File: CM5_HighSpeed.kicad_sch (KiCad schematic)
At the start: 15 parts, among them J12 USB3_A, J13 USB3_A, J15 USB_C_Receptacle_USB2.0, J22 690-019-298-412, J5 Conn_01x22_Female, U12 RT9742SNGV, U6 AP22653W6

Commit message: starting to trace
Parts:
- removed J15: USB_C_Receptacle_USB2.0, Connector_USB:USB_C_Receptacle_GCT_USB4105-xx-A_16P_TopMnt_Horizontal, symbol Connector:USB_C_Receptacle_USB2.0_16P
- added C32, C33: 0.1 µF, Capacitor_SMD:C_0402_1005Metric, symbol Device:C_Small
- added C34, C46: 10u, Capacitor_SMD:C_0402_1005Metric, symbol Device:C
- added C35, C36, C37, C38, C39, C40, C41, C42, C43, C44, C45: 0.1u, Capacitor_SMD:C_0402_1005Metric, symbol Device:C
- added C47, C48: 1u, Capacitor_SMD:C_0402_1005Metric, symbol Device:C
- added C49: 100nF, Capacitor_SMD:C_0402_1005Metric, symbol Device:C
- added C50: 0.1uF, Capacitor_SMD:C_0402_1005Metric, symbol Device:C
- added FB1, FB2: 220 at 100Mhz, libreboard:BEADC1005X55N, symbol Device:FerriteBead_Small
- added J1, J10, J17, J6: 2169890001, libreboard:216989-0001_MOL, symbol MOLEX_2169890001:2169890001
- added J15: USB_C_Receptacle, Connector_USB:USB_C_Receptacle_Molex_105450-0101, symbol Connector:USB_C_Receptacle
- added R25, R26, R34, R35, R36, R37, R38, R39, R40, R41: 5.1 k, Resistor_SMD:R_0402_1005Metric, symbol Device:R_Small
- added R27: 9.53k 1%, Resistor_SMD:R_0402_1005Metric, symbol Device:R_Small
- added R28: 4.7k, Resistor_SMD:R_0402_1005Metric, symbol Device:R_Small
- added R33: 10k, Resistor_SMD:R_0402_1005Metric, symbol Device:R_Small
- added U11: TUSB4041I, Package_QFP:HTQFP-64-1EP_10x10mm_P0.5mm_EP8x8mm_Mask4.4x4.4mm_ThermalVias, symbol Interface_USB:TUSB4041I
- added U13: TLV73311PDBV, Package_TO_SOT_SMD:SOT-23-5, symbol Regulator_Linear:TLV73311PDBV
- added Y1: ECS-2520MV-240-CN-TR, Oscillator:Oscillator_SMD_ECS_2520MV-xxx-xx-4Pin_2.5x2.0mm, symbol Oscillator:ECS-2520MV-xxx-xx
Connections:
- net +3.3v: now also C48.2, C50.2, FB1.1, R25.2, R26.2, R28.1, R33.2, U13.1 (IN), U13.3 (EN), Y1.4 (VDD)
- net GND: now also C32.1, C33.2, C34.2, C35.2, C36.2, C37.2, C38.2, C39.2, C40.2, C41.2, C42.2, C43.2, C44.2, C45.2, C46.2, C47.1, C48.1, C49.1, C50.1, J1.A1 (GND), J1.A12 (GND), J1.B1 (GND), J1.B12 (GND), J10.A1 (GND), J10.A12 (GND), J10.B1 (GND), J10.B12 (GND), J15.A1 (GND), J15.A12 (GND), J15.B1 (GND), J15.B12 (GND), J15.S1 (SHIELD), J17.A1 (GND), J17.A12 (GND), J17.B1 (GND), J17.B12 (GND), J6.A1 (GND), J6.A12 (GND), J6.B1 (GND), J6.B12 (GND), R27.2, R34.2, R35.2, R36.2, R37.2, R38.1, R39.1, R40.1, R41.1, U13.2 (GND), Y1.2 (GND)
- net USB3-0-D_N: now also J15.A7 (D-), J15.B7 (D-); no longer J12.A2 (D-)
- net USB3-0-D_P: now also J15.A6 (D+), J15.B6 (D+); no longer J12.A3 (D+)
- net USB3-0-RX_N: now also J15.B10 (RX1-); no longer J12.A6 (SSRX+)
- net USB3-0-RX_P: now also J15.B11 (RX1+); no longer J12.A5 (SSRX-)
- net USB3-0-TX_N: now also J15.A3 (TX1-); no longer J12.A9 (SSTX+)
- net USB3-0-TX_P: now also J15.A2 (TX1+); no longer J12.A8 (SSTX-)
- net USB3-1-D_N: now also U11.22 (USB_DM_UP); no longer J12.B2 (D-)
- net USB3-1-D_P: now also U11.21 (USB_DP_UP); no longer J12.B3 (D+)
- net USB3-1-RX_N: no longer J12.B6 (SSRX+)
- net USB3-1-RX_P: no longer J12.B5 (SSRX-)
- net USB3-1-TX_N: no longer J12.B9 (SSTX+)
- net USB3-1-TX_P: no longer J12.B8 (SSTX-)
- net VBUS: now also J1.A4 (VBUS), J1.A9 (VBUS), J1.B4 (VBUS), J1.B9 (VBUS), J10.A4 (VBUS), J10.A9 (VBUS), J10.B4 (VBUS), J10.B9 (VBUS), J15.A4 (VBUS), J15.A9 (VBUS), J15.B4 (VBUS), J15.B9 (VBUS), J17.A4 (VBUS), J17.A9 (VBUS), J17.B4 (VBUS), J17.B9 (VBUS), J6.A4 (VBUS), J6.A9 (VBUS), J6.B4 (VBUS), J6.B9 (VBUS), U11.16 (USB_VBUS)
- new net: C39.1, C40.1, C41.1, C42.1, C43.1, C44.1, C45.1, C46.1, FB2.1, U11.19 (VDD), U11.25 (VDD), U11.37 (VDD), U11.45 (VDD), U11.53 (VDD), U11.60 (VDD), U11.63 (VDD)
- new net: R27.1, U11.32 (USB_R1)
- new net: C49.2, R33.1, U11.18 (GRSTz)
- new net: J1.A5 (CC1), R34.1
- new net: J1.A6 (DP1), J1.B6 (DP2), U11.33 (USB_DP_DN1)
- new net: J1.A7 (DN1), J1.B7 (DN2), U11.34 (USB_DM_DN1)
- new net: J1.B5 (CC2), R41.2
- new net: J10.B5 (CC2), R39.2
- new net: J15.A5 (CC1), R25.1
- new net: J17.A5 (CC1), R37.1
- new net: J6.A5 (CC1), R35.1
- new net: J6.B5 (CC2), R40.2
- new net: C34.1, C35.1, C36.1, C37.1, C38.1, FB1.2, U11.2 (VDD33), U11.20 (VDD33), U11.31 (VDD33), U11.48 (VDD33)
- new net: J10.A5 (CC1), R36.1
- new net: J17.B5 (CC2), R38.2
- new net: C33.1, J15.A10 (RX2-)
- new net: C32.2, J15.A11 (RX2+)
- new net: J15.B5 (CC2), R26.1
- new net: C47.2, FB2.2, U13.5 (OUT)
- new net: U11.30 (XI), Y1.3 (OUT)
- new net: R28.2, U11.8 (FULLPWRMGMTz/SMBA1)
- new net: J6.A6 (DP1), J6.B6 (DP2), U11.41 (USB_DP_DN2)
- new net: J6.A7 (DN1), J6.B7 (DN2), U11.42 (USB_DM_DN2)
- new net: J10.A6 (DP1), J10.B6 (DP2), U11.49 (USB_DP_DN3)
- new net: J10.A7 (DN1), J10.B7 (DN2), U11.50 (USB_DM_DN3)
- new net: J17.A6 (DP1), J17.B6 (DP2), U11.56 (USB_DP_DN4)
- new net: J17.A7 (DN1), J17.B7 (DN2), U11.57 (USB_DM_DN4)
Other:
- moved on the sheet: J12, J13

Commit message: fully traced
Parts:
- removed J12, J13: USB3_A, CM5IO:MTCONN_UBAF30-D2011, symbol CM5IO:USB3_A
- added C56, C58, C59: 10u, Capacitor_SMD:C_0805_2012Metric, symbol Device:C
- added C57: 100uF, Capacitor_Tantalum_SMD:CP_EIA-7343-31_Kemet-D, symbol Device:C_Polarized
- added R46: 15K 1%, Resistor_SMD:R_0402_1005Metric, symbol Device:R
- added U15: AP22653W6, Package_TO_SOT_SMD:SOT-23-6, symbol CM5IO:AP2553W6
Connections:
- net +5v: now also C56.1, U15.1 (IN)
- net GND: now also C56.2, C57.2, C58.2, C59.2, R46.2, U15.2 (GND)
- net VBUS_EN: now also U15.3 (EN)
- net VBUS renamed USB2_VBUS
- net USB2_VBUS: no longer J15.A4 (VBUS), J15.A9 (VBUS), J15.B4 (VBUS), J15.B9 (VBUS)
- new net: R46.1, U15.5 (ILIM)
- new net USB3_VBUS: C57.1, C58.1, C59.1, J15.A4 (VBUS), J15.A9 (VBUS), J15.B4 (VBUS), J15.B9 (VBUS), U15.6 (OUT)
- no-connect marks 2 -> 3

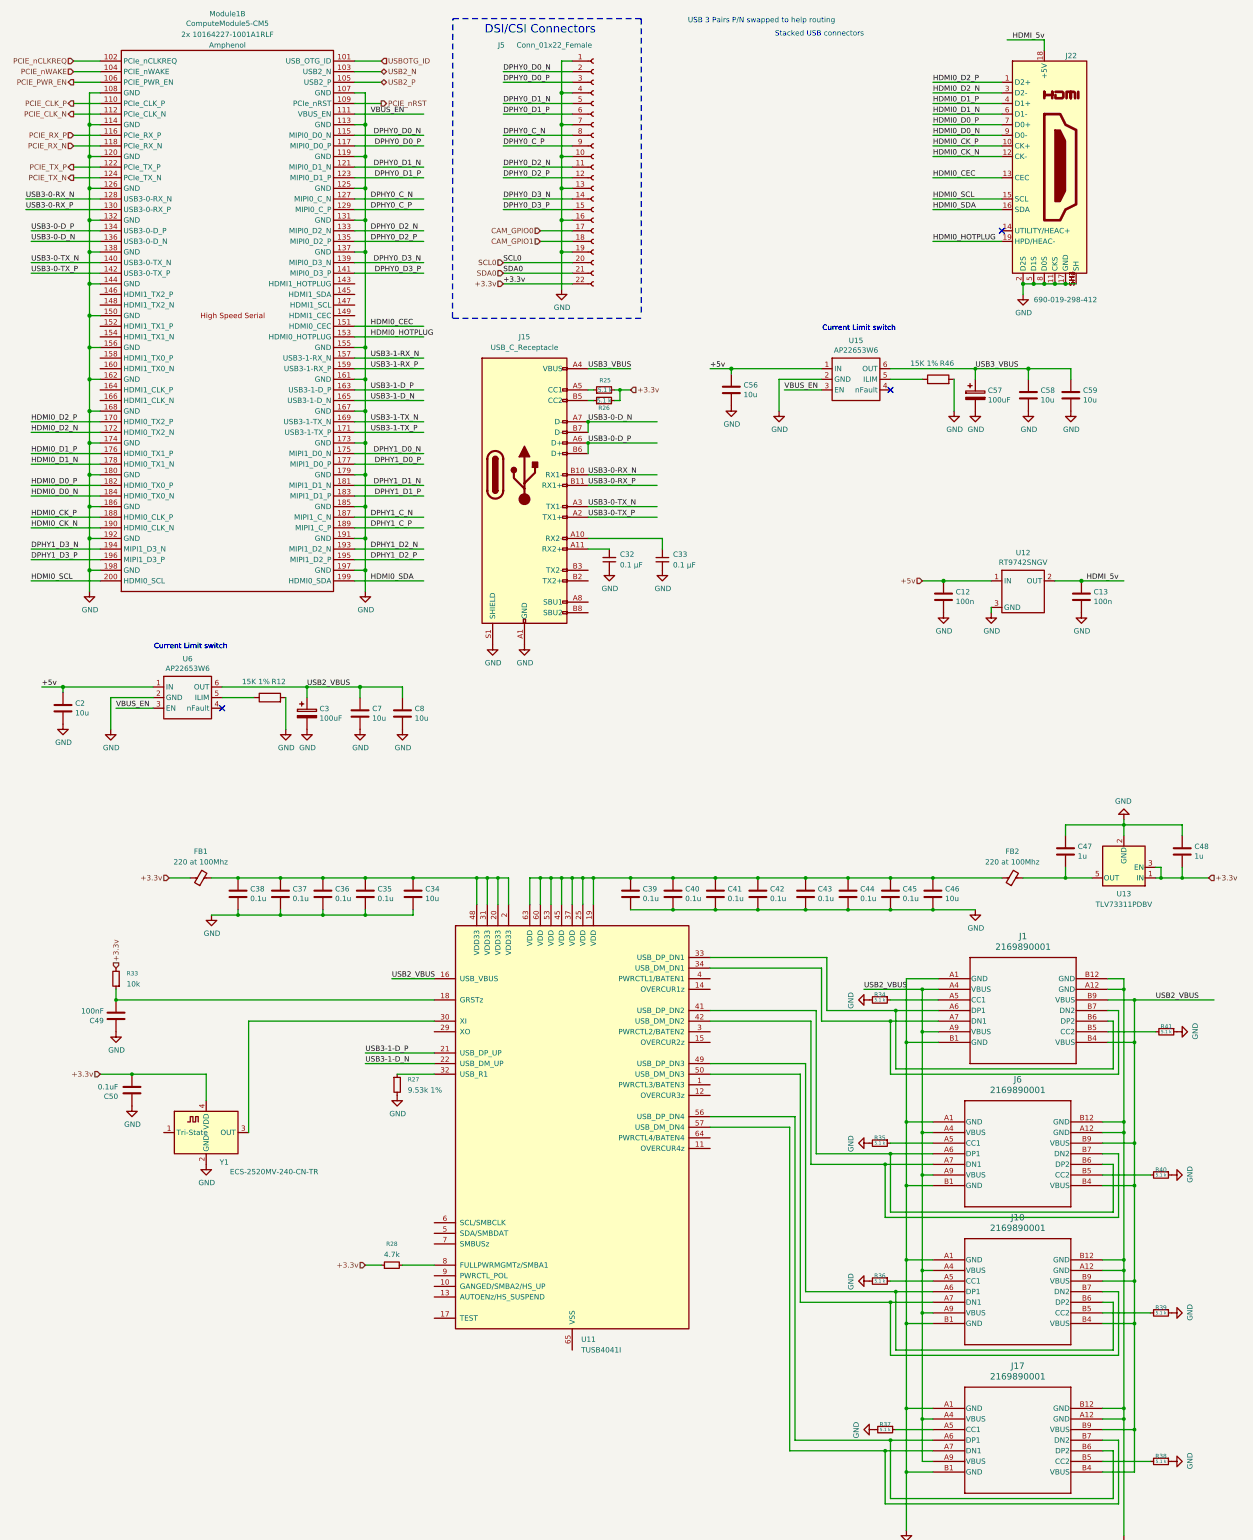
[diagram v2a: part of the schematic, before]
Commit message: voltage regulator refactoring
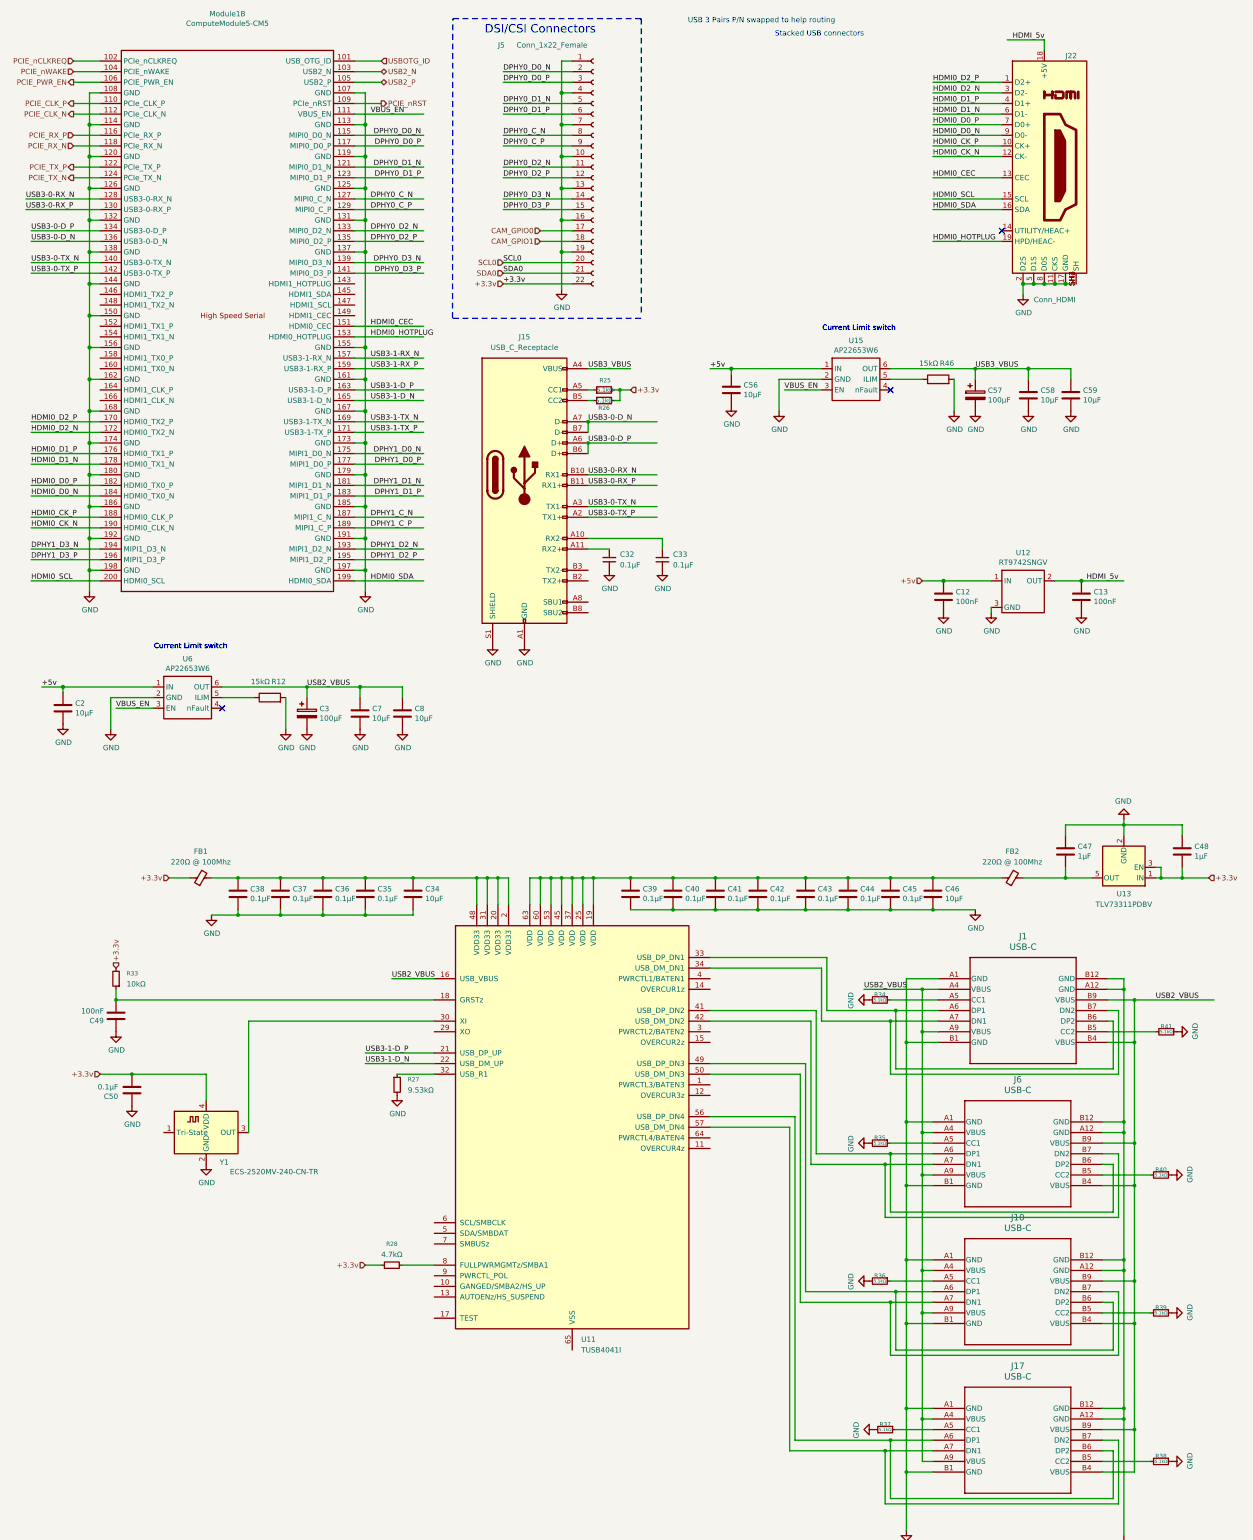
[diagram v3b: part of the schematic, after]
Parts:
- C12, C13: value 100n -> 100nF; Dist. P/N (none) -> 478-11504-2-ND; Distributor (none) -> Digikey; Field4 Farnell -> (none); Field5 2611911 -> (none); Field6 RM EMK105 B7104KV-F -> (none); Field7 TAIYO YUDEN EUROPE GMBH -> (none); Field8 110091611 -> (none); Manf. P/N (none) -> 04026D104KAT4A; Manufacturer (none) -> Kyocera; Part Description 0.1uF 10% 16V Ceramic Capacitor X7R 0402 (1005 Metric) -> Capacitor, Ceramic, 0.1µF, ±10%, 6.3V, X5R, 0402 (1005m)
- C2, C56, C58, C59, C7, C8: value 10u -> 10µF; Dist. P/N (none) -> 478-KGM21AR51A106KUTR-ND; Distributor (none) -> Digikey; Field4 Digikey -> (none); Field5 490-14381-1-ND -> (none); Field6 GRM21BR71A106KA73L -> (none); Field7 Murata -> (none); Field8 111893011 -> (none); Manf. P/N (none) -> 0805ZD106KAT2A; Manufacturer (none) -> Kyocera; Part Description 10uF 10% 10V Ceramic Capacitor X7R 0805 (2012 Metric) -> Capacitor, Ceramic, 10µF, ±10%, 10V, X5R, 0805 (2012m)
- C3, C57: value 100uF -> 100µF; Dist. P/N (none) -> 399-11382-2-ND; Distributor (none) -> Digikey; Field4 Mouser -> (none); Field5 667-EEF-CX0J101R -> (none); Field7 Panasonic -> (none); Manf. P/N (none) -> A700X107M010ATE010; Manufacturer (none) -> Kemet; Part Description Capacitor, SP-Cap, 100u, 6.3V, 15mR ESR -> Capacitor, AO-Cap, 100µF, ±20%, 10V, 10mΩ ESR
- C32, C33: value 0.1 µF -> 0.1µF; Dist. P/N (none) -> 478-11504-2-ND; Distributor (none) -> Digikey; Manf. P/N (none) -> 04026D104KAT4A; Manufacturer (none) -> Kyocera; Part Description (none) -> Capacitor, Ceramic, 0.1µF, ±10%, 6.3V, X5R, 0402 (1005m)
- C34, C46: value 10u -> 10µF; Dist. P/N (none) -> 478-KGM05CR50J106MHTR-ND; Distributor (none) -> Digikey; Field4 Digikey -> (none); Field5 490-14381-1-ND -> (none); Field6 GRM21BR71A106KA73L -> (none); Field7 Murata -> (none); Field8 111893011 -> (none); Manf. P/N (none) -> 04026D106MAT2A; Manufacturer (none) -> Kyocera; Part Description 10uF 10% 10V Ceramic Capacitor X7R 0805 (2012 Metric) -> Capacitor, Ceramic, 10µF, ±20%, 6.3V, X5R, 0402 (1005m)
- C35, C36, C37, C38, C39, C40, C41, C42, C43, C44, C45: value 0.1u -> 0.1µF; Dist. P/N (none) -> 478-11504-2-ND; Distributor (none) -> Digikey; Field4 Digikey -> (none); Field5 490-14381-1-ND -> (none); Field6 GRM21BR71A106KA73L -> (none); Field7 Murata -> (none); Field8 111893011 -> (none); Manf. P/N (none) -> 04026D104KAT4A; Manufacturer (none) -> Kyocera; Part Description 10uF 10% 10V Ceramic Capacitor X7R 0805 (2012 Metric) -> Capacitor, Ceramic, 0.1µF, ±10%, 6.3V, X5R, 0402 (1005m)
- C47, C48: value 1u -> 1µF; Dist. P/N (none) -> 478-KGM05AR50J105KHTR-ND; Distributor (none) -> Digikey; Field4 Digikey -> (none); Field5 490-14381-1-ND -> (none); Field6 GRM21BR71A106KA73L -> (none); Field7 Murata -> (none); Field8 111893011 -> (none); Manf. P/N (none) -> 04026D105KAT2A; Manufacturer (none) -> Kyocera; Part Description 10uF 10% 10V Ceramic Capacitor X7R 0805 (2012 Metric) -> Capacitor, Ceramic, 1µF, ±10%, 6.3V, X5R, 0402 (1005m)
- C49: Dist. P/N (none) -> 478-11504-2-ND; Distributor (none) -> Digikey; Field4 Digikey -> (none); Field5 490-14381-1-ND -> (none); Field6 GRM21BR71A106KA73L -> (none); Field7 Murata -> (none); Field8 111893011 -> (none); Manf. P/N (none) -> 04026D104KAT4A; Manufacturer (none) -> Kyocera; Part Description 10uF 10% 10V Ceramic Capacitor X7R 0805 (2012 Metric) -> Capacitor, Ceramic, 0.1µF, ±10%, 6.3V, X5R, 0402 (1005m)
- C50: value 0.1uF -> 0.1µF; Dist. P/N (none) -> 478-11504-2-ND; Distributor (none) -> Digikey; Field4 Digikey -> (none); Field5 490-14381-1-ND -> (none); Field6 GRM21BR71A106KA73L -> (none); Field7 Murata -> (none); Field8 111893011 -> (none); Manf. P/N (none) -> 04026D104KAT4A; Manufacturer (none) -> Kyocera; Part Description 10uF 10% 10V Ceramic Capacitor X7R 0805 (2012 Metric) -> Capacitor, Ceramic, 0.1µF, ±10%, 6.3V, X5R, 0402 (1005m)
- FB1, FB2: value 220 at 100Mhz -> 220Ω @ 100Mhz; Dist. P/N (none) -> 240-2554-2-ND; Distributor (none) -> Digikey; Manf. P/N (none) -> LI0402C221R-10; Manufacturer (none) -> Laird Signal; Part Description (none) -> Filter, Ferrite Bead, 220Ω @ 100MHz, SMD 0402
- J1, J10, J17, J6: value 2169890001 -> USB-C; Dist. P/N (none) -> 900-2169890001TR-ND; Distributor (none) -> Digikey; Manf. P/N (none) -> 2169890001; Manufacturer (none) -> Molex; Part Description (none) -> Receptacle, USB-C, 2.0, 24 pin (14+10 Dummy), Through Hole,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
- J15: Dist. P/N (none) -> WM12856TR-ND; Distributor (none) -> Digikey; Manf. P/N (none) -> 1054500101; Manufacturer (none) -> Molex; Part Description (none) -> Connector, USB-C 3.2 Gen 2
- J22: value 690-019-298-412 -> Conn_HDMI; Dist. P/N (none) -> 900-2086581051TR-ND; Distributor (none) -> Digikey; Field4 Farnell -> (none); Field5 2614936 -> (none); Field6 690-019-298-412 -> (none); Field7 EDAC -> (none); Field8 UCON00802 -> (none); Manf. P/N (none) -> 2086581051; Manufacturer (none) -> Molex; Part Description HDMI Connector, Right Angle, 19 Contacts, Receptacle, Surfa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 -> Connector, HDMI 2.1, Female, Right Angle, 19 pin, SMD
- J5: value Conn_01x22_Female -> Conn_1x22_Female; Dist. P/N (none) -> HFJ122TR-ND; Distributor (none) -> Digikey; Field4 Mouser -> (none); Field5 798-FH12-22S-0.5SH55 -> (none); Field6 FH12-22S-0.5SH55 -> (none); Field7 Hirose -> (none); Manf. P/N (none) -> FH12-22S-0.5SH55; Manufacturer (none) -> Hirose; Part Description 22 Position FFC, FPC Connector Contacts, Bottom 0.020" (0.5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 -> Connector, 22 Position FFC, FPC Connector Contacts, Bottom 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
- Module1: Dist. P/N (none) -> 609-10164227-1001A1RLFTR-ND; Distributor (none) -> Digikey; Field4 Amphenol -> (none); Field5 2x 10164227-1001A1RLF -> (none); Field6 2x 10164227-1001A1RLF -> (none); Field7 Hirose -> (none); Manf. P/N (none) -> 10164227-1001A1RLF x2; Manufacturer (none) -> Amphenol; Part Description 100 Position Connector Receptacle, Center Strip Contacts Su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 -> Connector, CM Receptacle, 100 pin, 0.4mm P
- R12, R46: value 15K 1% -> 15kΩ; Dist. P/N (none) -> P15.0KLTR-ND; Distributor (none) -> Digikey; Field4 Farnell -> (none); Field5 9239375 -> (none); Field6 MCR01MZPF1502 -> (none); Field7 Rohm -> (none); Field8 120891581 -> (none); Manf. P/N (none) -> ERJ-2RKF1502X; Manufacturer (none) -> Panasonic; Part Description Resistor 15K M1005 1% 63mW -> Resistor, 15kΩ, ±1%, 0.1W, SMD 0402 (1005m)
- R25, R26, R34, R35, R36, R37, R38, R39, R40, R41: value 5.1 k -> 5.1kΩ; Dist. P/N (none) -> P5.10KLTR-ND; Distributor (none) -> Digikey; Manf. P/N (none) -> ERJ-2RKF5101X; Manufacturer (none) -> Panasonic; Part Description (none) -> Resistor, 5.1kΩ, ±1%, 0.1W, SMD 0402 (1005m)
- R27: value 9.53k 1% -> 9.53kΩ; Dist. P/N (none) -> P9.53KLTR-ND; Distributor (none) -> Digikey; Manf. P/N (none) -> ERJ-2RKF9531X; Manufacturer (none) -> Panasonic; Part Description (none) -> Resistor, 9.53kΩ, ±1%, 0.1W, SMD 0402 (1005m)
- R28: value 4.7k -> 4.7kΩ; Dist. P/N (none) -> 10-ERJ-U02F4701XTR-ND; Distributor (none) -> Digikey; Manf. P/N (none) -> ERJ-U02F4701X; Manufacturer (none) -> Panasonic; Part Description (none) -> Resistor, 4.7kΩ, ±1%, 0.1W, SMD 0402 (1005m)
- R33: value 10k -> 10kΩ; Dist. P/N (none) -> 10-ERJ-U02F1002XTR-ND; Distributor (none) -> Digikey; Manf. P/N (none) -> ERJ-U02F1002X; Manufacturer (none) -> Panasonic; Part Description (none) -> Resistor, 10kΩ, ±1%, 0.1W, SMD 0402 (1005m)
- U11: Dist. P/N (none) -> 296-43143-2-ND; Distributor (none) -> Digikey; Manf. P/N (none) -> TUSB4041IPAPR; Manufacturer (none) -> Texas Instruments; Part Description (none) -> Controller, USB Hub, 64-HTQFP
- U12: Dist. P/N (none) -> 1028-RT9742SNGVTR-ND; Distributor (none) -> Digikey; Field4 Farnell -> (none); Field5 2575555 -> (none); Field6 RT9742SNGV -> (none); Field7 RichTek -> (none); Field8 USWI00155 -> (none); Manf. P/N (none) -> RT9742SNGV; Manufacturer (none) -> RichTek; Part Description Power Switch/Driver 1:1 N-Channel 500mA SOT-23-3 -> Power Switch/Driver, 1:1, N-Channel, 500mA, SOT-23-3
- U13: Dist. P/N (none) -> 296-38620-2-ND; Distributor (none) -> Digikey; Manf. P/N (none) -> TLV73311PDBVT; Manufacturer (none) -> Texas Instruments; Part Description (none) -> LVR, IC Positive Fixed, 1 Output, 300mA, SOT-23-5
- U15, U6: Dist. P/N (none) -> 31-AP22653W6-7TR-ND; Distributor (none) -> Digikey; Field4 Digikey -> (none); Field5 31-AP22653W6-7CT-ND -> (none); Field6 AP22653W6 -> (none); Field7 Diodes -> (none); Manf. P/N (none) -> AP22653W6-7; Manufacturer (none) -> Diodes Inc.; Part Description Power Switch/Driver 1:1 P-Channel 2.1A SOT-23-6 -> Power Switch/Driver, 1:1, P-Channel, 2.1A, SOT-23-6
- Y1: Dist. P/N (none) -> 50-ECS-2520MV-240-DN-TR-ND; Distributor (none) -> Digikey; Manf. P/N (none) -> ECS-2520MV-240-DN-TR; Manufacturer (none) -> ECS Inc.; Part Description (none) -> Oscillator, 24MHz, 1.6V~3.6V

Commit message: updates BOM, sychronizes PCB from schematic, & includes error report.
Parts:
- C3, C57: Part Description Capacitor, AO-Cap, 100µF, ±20%, 10V, 10mΩ ESR -> Capacitor, Aluminum, 100µF, ±20%, 10V, 10mΩ ESR
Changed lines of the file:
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@@
 			)
 		)
-		(property "Part Description" "Capacitor, AO-Cap, 100µF, ±20%, 10V, 10mΩ ESR"
+		(property "Part Description" "Capacitor, Aluminum, 100µF, ±20%, 10V, 10mΩ ESR"
 			(at 87.63 181.61 0)
 			(effects
@@
 			)
 		)
-		(property "Part Description" "Capacitor, AO-Cap, 100µF, ±20%, 10V, 10mΩ ESR"
+		(property "Part Description" "Capacitor, Aluminum, 100µF, ±20%, 10V, 10mΩ ESR"
 			(at 247.65 105.41 0)
 			(effects

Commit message: cleanup, testpoints
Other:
- moved on the sheet: C12, C13, C32, C33, C34, C35, C36, C37, C38, C39, C40, C41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

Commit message: final review, added coincell back, additional testpoints, updated i2c bus for quic
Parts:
- J1, J10, J17, J6: footprint libreboard:216989-0001_MOL -> 216989-0001_MOL
- J22: footprint CM5IO:EDAC 690-019-298-412 -> libreboard:EDAC 690-019-298-412
- J5: footprint CM5IO:Hirose_FH12-22S-0.5SH_1x22-1MP_P0.50mm_Horizontal -> libreboard:Hirose_FH12-22S-0.5SH_1x22-1MP_P0.50mm_Horizontal
- Module1: footprint CM5IO:Raspberry-Pi-5-Compute-Module -> libreboard:Raspberry-Pi-5-Compute-Module
